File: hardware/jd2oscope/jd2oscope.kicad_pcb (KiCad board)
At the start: 4 copper layers, 83 x 120 mm, 61 parts, among them J1 9V_CONN, J2 CONBNC001, J3 CONBNC001, U1 ESP32-DEVKITC-32D, U2 ILI9341-320x240-TFT-Touch, U3 NCP1117-5.0_SOT223, U4 OPA192IDBVR, U5 ADS7279IPW, U6 OPA192IDBVR, U7 ADS7279IPW

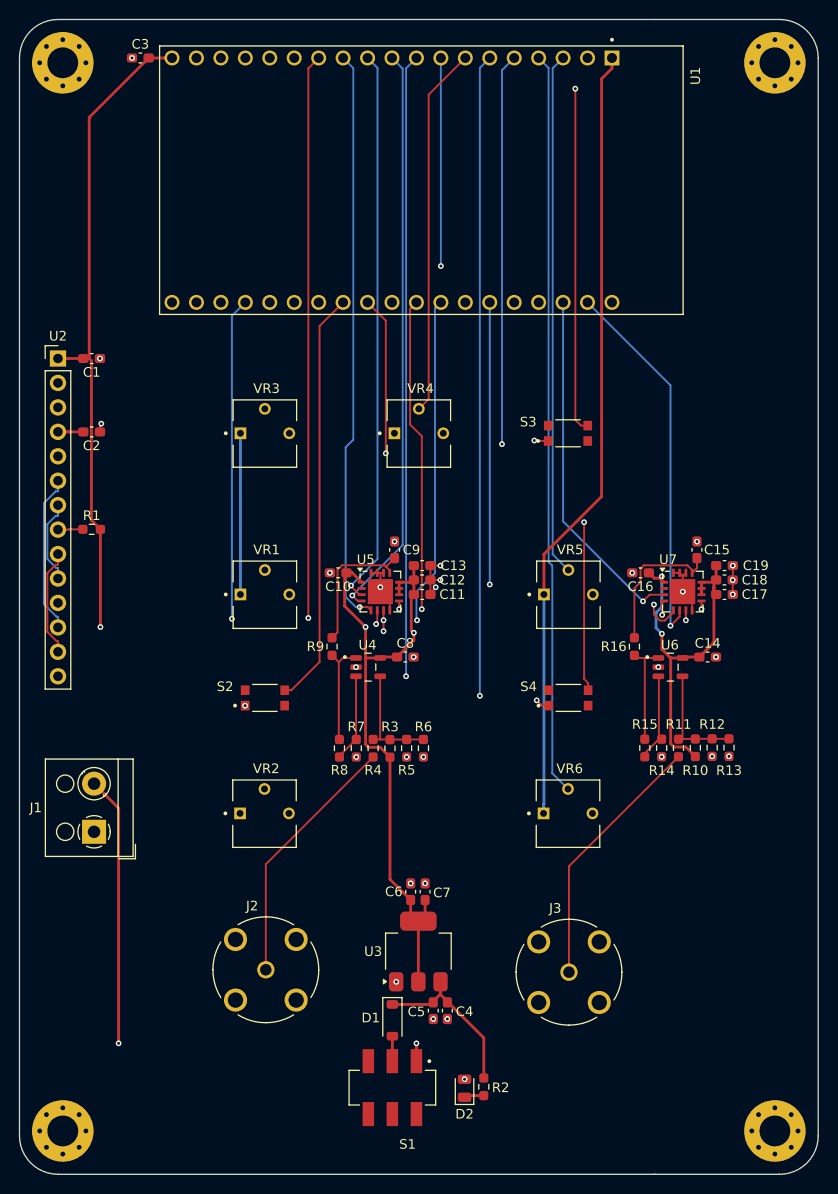
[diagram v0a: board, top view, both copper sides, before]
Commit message: feat: silkscreen updates
note that DRC now produces warnings for some of the silkscreens on the back of the PCB. I am under the impression that they don't matter that much, & hoping it "just works"; if anything, minor bleed or inconsistencies in the text will be present (if silkscreen tolerances sabotage electrical continuity and the pcb doesn't work (*when they are close to no traces*), guess I deserved this one lol. But it SHOULD be fine!!)
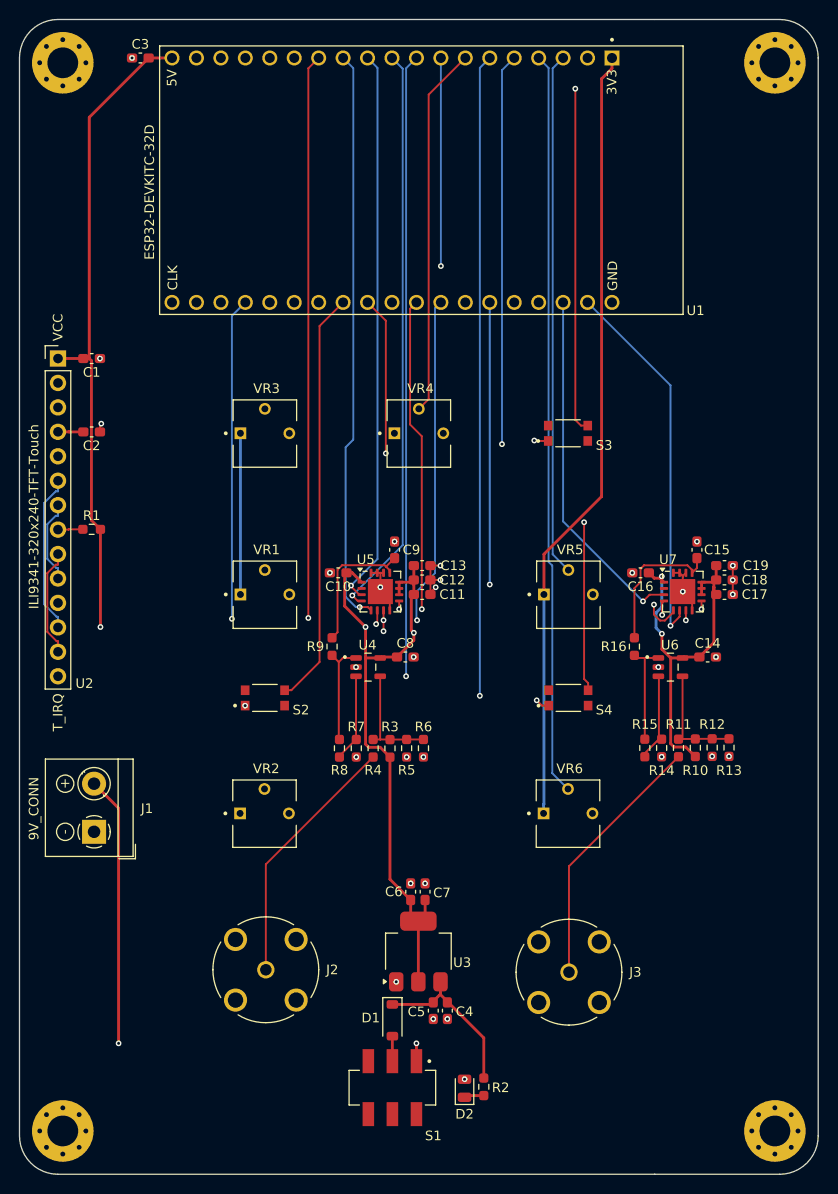
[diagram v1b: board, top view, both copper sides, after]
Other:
- board text added: "(March 2025)"
- board text added: "+"
- board text added: "-"
- board text added: "3V3"
- board text added: "5V"
- board text added: "CLK"
- board text added: "ECE 342 - 2CH 1MS/s, 12-Bit, 50kHz Oscope (5V) w/320x240 TFT & ESP32"
- board text added: "GND"
- board text added: "JLCJLCJLCJLC"
- board text added: "Kayla Uyema Noah Fontenot Wesley Grandmont IV"
- board text added: "T_IRQ"
- board text added: "VCC"
- board text added: "v.1"
- board text added: "☯"
